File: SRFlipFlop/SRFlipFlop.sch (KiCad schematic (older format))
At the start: 5 parts, among them U1 74LS08, U2 74LS08, U3 74LS02, U4 74LS04

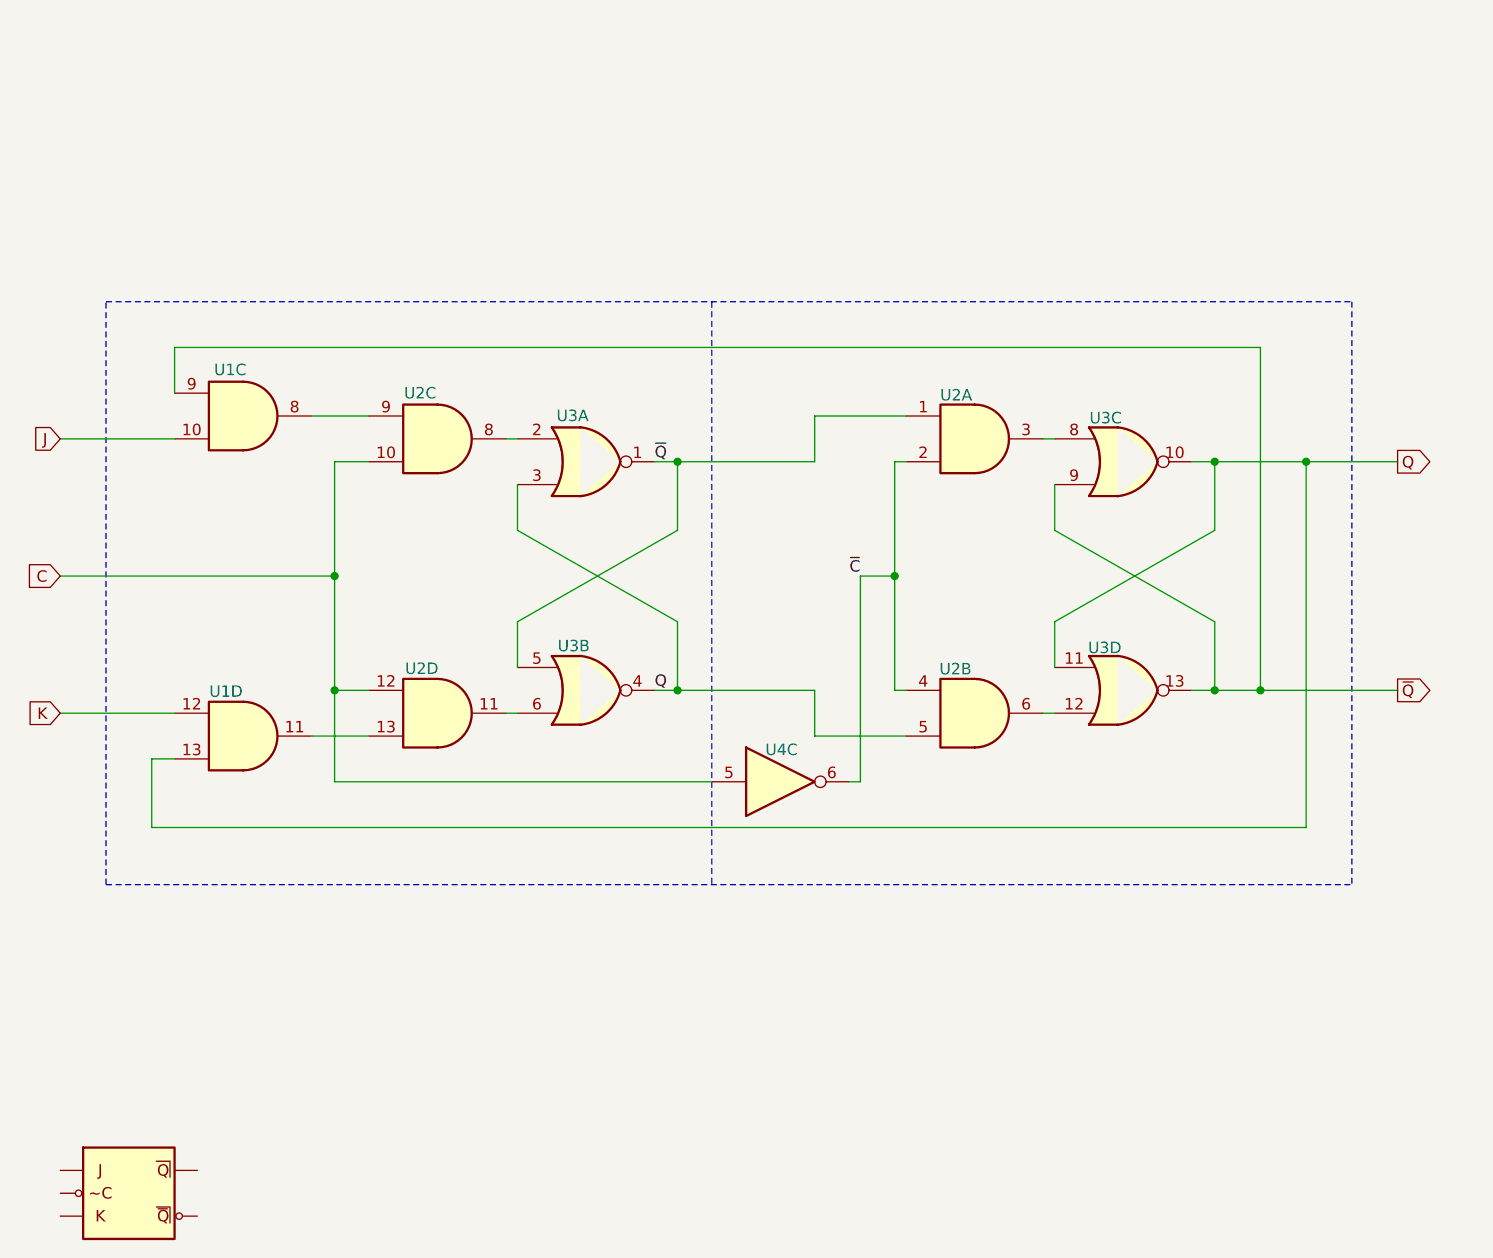
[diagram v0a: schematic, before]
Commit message: fix S/R latch
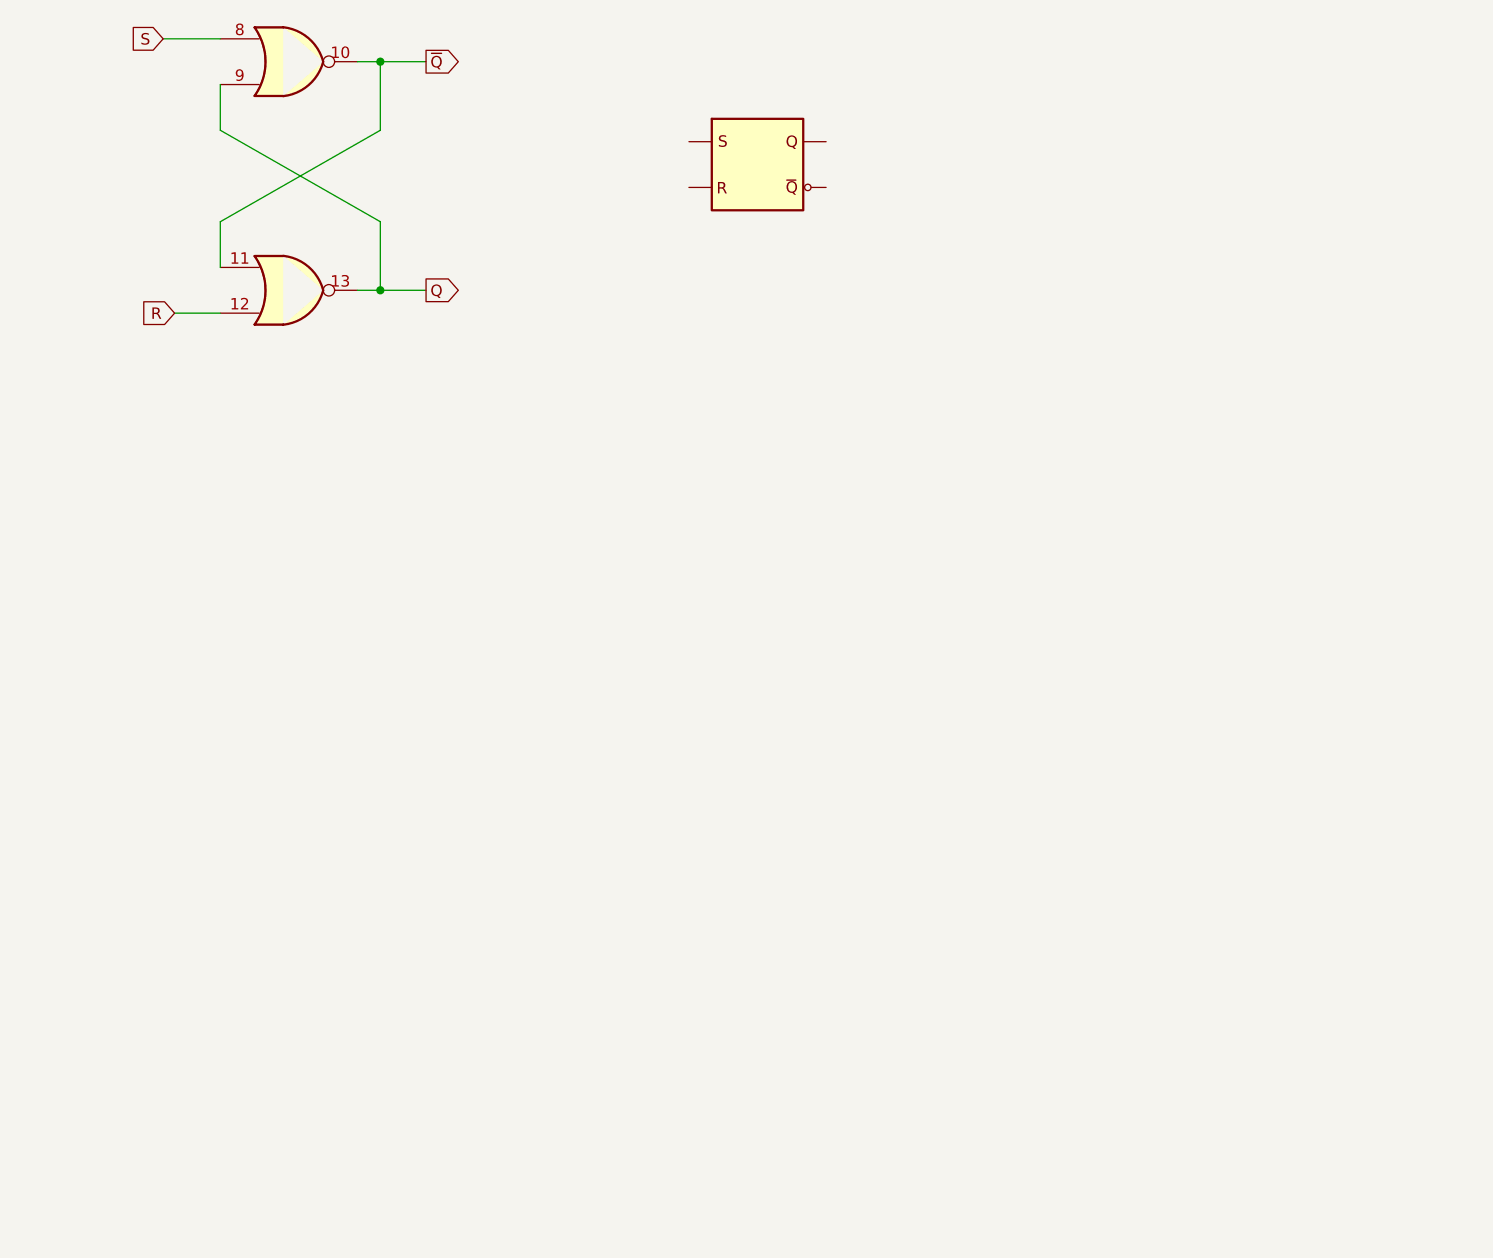
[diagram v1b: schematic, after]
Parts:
- removed U1, U2: 74LS08, symbol 74xx:74LS08
- removed unit 1 of U3
- removed unit 2 of U3
- removed U4: 74LS04, symbol 74xx:74LS04
- removed U?: JK_MS, symbol 00TJR:JK_MS
- added U?: SR_Latch, symbol 00TJR:SR_Latch
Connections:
- net Q: now also U3.13, U3.9; no longer U3.10, U3.11
- net ~Q: now also U3.10, U3.11; no longer U3.13, U3.9
- net R: now reaches U3.12
- net S: now reaches U3.8
